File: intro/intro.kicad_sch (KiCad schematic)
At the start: 4 parts, among them SW1 SW_Push

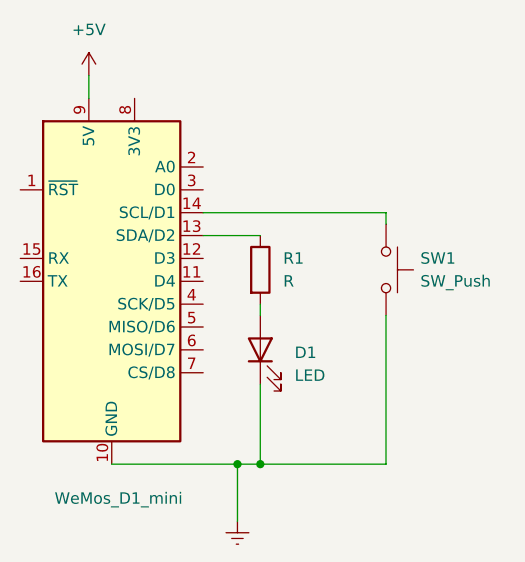
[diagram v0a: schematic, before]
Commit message: Start migration of wiring to KiCAD
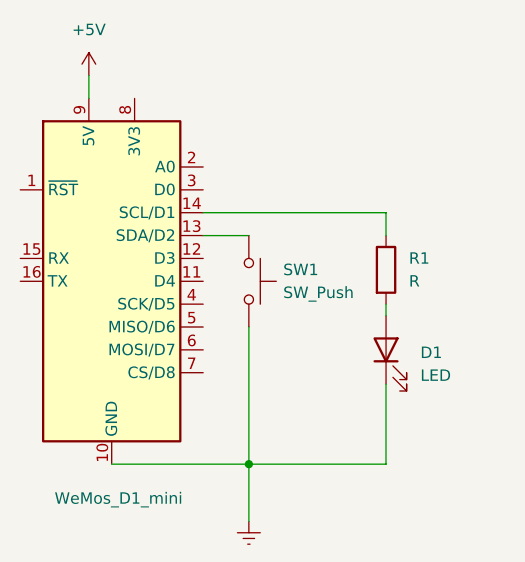
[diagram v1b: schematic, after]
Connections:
- net at R1.1: now also U?.14 (SCL/D1); no longer U?.13 (SDA/D2)
- net at SW1.1: now also U?.13 (SDA/D2); no longer U?.14 (SCL/D1)
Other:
- moved on the sheet: D1, R1, SW1
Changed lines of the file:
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@@
 (kicad_sch (version 20211123) (generator eeschema)
   (paper "A4")
-  (junction (at 110.49 107.95) (diameter 0) (color 0 0 0 0)
+  (junction (at 111.76 107.95) (diameter 0) (color 0 0 0 0)
   )
-  (junction (at 113.03 107.95) (diameter 0) (color 0 0 0 0)
+  (wire (pts (xy 127 82.55) (xy 127 80.01))
+    (stroke (width 0) (type default) (color 0 0 0 0))
   )
-  (wire (pts (xy 96.52 107.95) (xy 110.49 107.95))
+  (wire (pts (xy 96.52 107.95) (xy 111.76 107.95))
+    (stroke (width 0) (type default) (color 0 0 0 0))
+  )
+  (wire (pts (xy 111.76 92.71) (xy 111.76 107.95))
+    (stroke (width 0) (type default) (color 0 0 0 0))
+  )
+  (wire (pts (xy 93.98 67.31) (xy 93.98 64.77))
+    (stroke (width 0) (type default) (color 0 0 0 0))
+  )
+  (wire (pts (xy 127 99.06) (xy 127 107.95))
     (stroke (width 0) (type default) (color 0 0 0 0))
   )
@@
     (stroke (width 0) (type default) (color 0 0 0 0))
   )
-  (wire (pts (xy 93.98 67.31) (xy 93.98 64.77))
+  (wire (pts (xy 127 90.17) (xy 127 91.44))
     (stroke (width 0) (type default) (color 0 0 0 0))
   )
-  (wire (pts (xy 113.03 99.06) (xy 113.03 107.95))
+  (wire (pts (xy 111.76 107.95) (xy 111.76 114.3))
     (stroke (width 0) (type default) (color 0 0 0 0))
   )
-  (wire (pts (xy 113.03 90.17) (xy 113.03 91.44))
+  (wire (pts (xy 106.68 82.55) (xy 111.76 82.55))
     (stroke (width 0) (type default) (color 0 0 0 0))
   )
-  (wire (pts (xy 127 91.44) (xy 127 107.95))
+  (wire (pts (xy 111.76 107.95) (xy 127 107.95))
     (stroke (width 0) (type default) (color 0 0 0 0))
   )
-  (wire (pts (xy 110.49 107.95) (xy 110.49 114.3))
-    (stroke (width 0) (type default) (color 0 0 0 0))
-  )
-  (wire (pts (xy 113.03 107.95) (xy 127 107.95))
-    (stroke (width 0) (type default) (color 0 0 0 0))
-  )
-  (wire (pts (xy 127 80.01) (xy 127 81.28))
-    (stroke (width 0) (type default) (color 0 0 0 0))
-  )
-  (wire (pts (xy 110.49 107.95) (xy 113.03 107.95))
-    (stroke (width 0) (type default) (color 0 0 0 0))
-  )
-  (wire (pts (xy 106.68 82.55) (xy 113.03 82.55))
-    (stroke (width 0) (type default) (color 0 0 0 0))
-  )
-  (symbol (lib_id "Device:R") (at 113.03 86.36 0) (unit 1)
+  (symbol (lib_id "Device:R") (at 127 86.36 0) (unit 1)
     (in_bom yes) (on_board yes)
-    (property "Reference" "R1" (id 0) (at 115.57 85.0899 0)
+    (property "Reference" "R1" (id 0) (at 129.54 85.0899 0)
       (effects (font (size 1.27 1.27)) (justify left))
     )
-    (property "Value" "R" (id 1) (at 115.57 87.6299 0)
+    (property "Value" "R" (id 1) (at 129.54 87.6299 0)
       (effects (font (size 1.27 1.27)) (justify left))
     )
-    (property "Footprint" "" (id 2) (at 111.252 86.36 90)
+    (property "Footprint" "" (id 2) (at 125.222 86.36 90)
       (effects (font (size 1.27 1.27)) hide)
     )
-    (property "Datasheet" "~" (id 3) (at 113.03 86.36 0)
+    (property "Datasheet" "~" (id 3) (at 127 86.36 0)
       (effects (font (size 1.27 1.27)) hide)
     )
@@
     (pin "2")
   )
-  (symbol (lib_id "power:Earth") (at 110.49 114.3 0) (unit 1)
+  (symbol (lib_id "power:Earth") (at 111.76 114.3 0) (unit 1)
     (in_bom yes) (on_board yes) (fields_autoplaced)
-    (property "Reference" "#PWR?" (id 0) (at 110.49 120.65 0)
+    (property "Reference" "#PWR?" (id 0) (at 111.76 120.65 0)
       (effects (font (size 1.27 1.27)) hide)
     )
-    (property "Value" "Earth" (id 1) (at 110.49 118.11 0)
+    (property "Value" "Earth" (id 1) (at 111.76 118.11 0)
       (effects (font (size 1.27 1.27)) hide)
     )
-    (property "Footprint" "" (id 2) (at 110.49 114.3 0)
+    (property "Footprint" "" (id 2) (at 111.76 114.3 0)
       (effects (font (size 1.27 1.27)) hide)
     )
-    (property "Datasheet" "~" (id 3) (at 110.49 114.3 0)
+    (property "Datasheet" "~" (id 3) (at 111.76 114.3 0)
       (effects (font (size 1.27 1.27)) hide)
     )
     (pin "1")
   )
-  (symbol (lib_id "Switch:SW_Push") (at 127 86.36 270) (unit 1)
-    (in_bom yes) (on_board yes) (fields_autoplaced)
-    (property "Reference" "SW1" (id 0) (at 130.81 85.0899 90)
+  (symbol (lib_id "Switch:SW_Push") (at 111.76 87.63 270) (unit 1)
+    (in_bom yes) (on_board yes)
+    (property "Reference" "SW1" (id 0) (at 115.57 86.3599 90)
       (effects (font (size 1.27 1.27)) (justify left))
     )
-    (property "Value" "SW_Push" (id 1) (at 130.81 87.6299 90)
+    (property "Value" "SW_Push" (id 1) (at 115.57 88.9 90)
       (effects (font (size 1.27 1.27)) (justify left))
     )
-    (property "Footprint" "" (id 2) (at 132.08 86.36 0)
+    (property "Footprint" "" (id 2) (at 116.84 87.63 0)
       (effects (font (size 1.27 1.27)) hide)
     )
-    (property "Datasheet" "~" (id 3) (at 132.08 86.36 0)
+    (property "Datasheet" "~" (id 3) (at 116.84 87.63 0)
       (effects (font (size 1.27 1.27)) hide)
     )
@@
     (pin "1")
   )
-  (symbol (lib_id "Device:LED") (at 113.03 95.25 90) (unit 1)
+  (symbol (lib_id "Device:LED") (at 127 95.25 90) (unit 1)
     (in_bom yes) (on_board yes) (fields_autoplaced)
-    (property "Reference" "D1" (id 0) (at 116.84 95.5674 90)
+    (property "Reference" "D1" (id 0) (at 130.81 95.5674 90)
       (effects (font (size 1.27 1.27)) (justify right))
     )
-    (property "Value" "LED" (id 1) (at 116.84 98.1074 90)
+    (property "Value" "LED" (id 1) (at 130.81 98.1074 90)
       (effects (font (size 1.27 1.27)) (justify right))
     )
-    (property "Footprint" "" (id 2) (at 113.03 95.25 0)
+    (property "Footprint" "" (id 2) (at 127 95.25 0)
       (effects (font (size 1.27 1.27)) hide)
     )
-    (property "Datasheet" "~" (id 3) (at 113.03 95.25 0)
+    (property "Datasheet" "~" (id 3) (at 127 95.25 0)
       (effects (font (size 1.27 1.27)) hide)
     )
